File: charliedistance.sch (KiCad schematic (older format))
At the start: 1 part, among them X1 Badgelife_sao_connector_v169b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

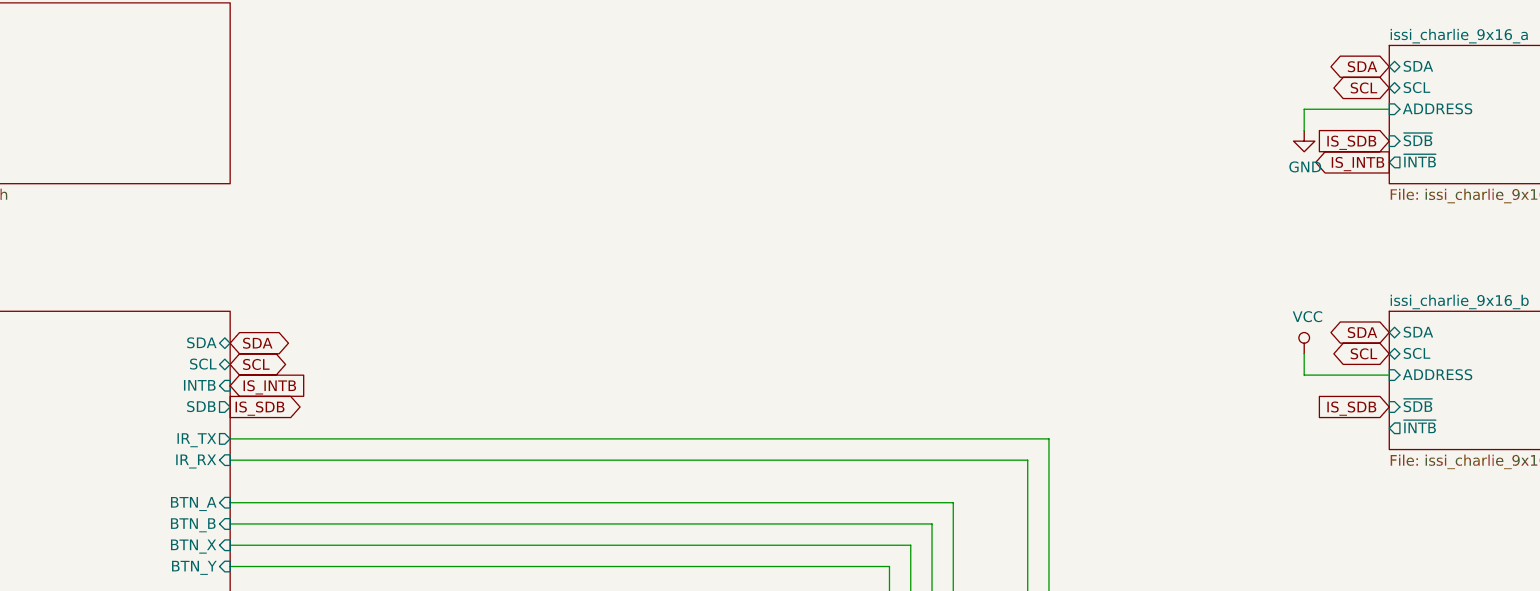
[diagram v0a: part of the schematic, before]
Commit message: Updates to production version
Changed infrared setup, added step-up for battery power, added battery power switch, added more capacitors, changed and added logos, etc.
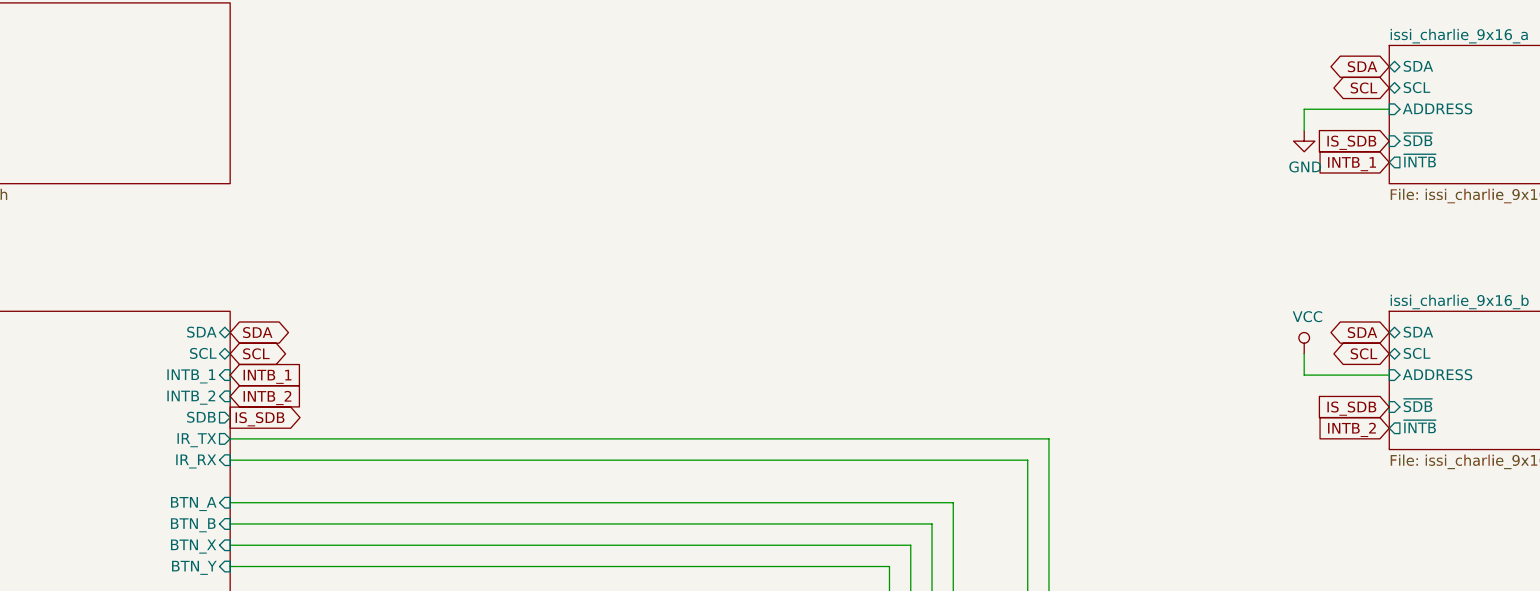
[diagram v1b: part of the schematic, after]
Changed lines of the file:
@@
 F2 "USB_BUS_POWER" I L 1100 1350 50
 $EndSheet
-Text GLabel 3100 2750 2    50   BiDi ~ 0
+Text GLabel 3100 2700 2    50   BiDi ~ 0
 SDA
-Text GLabel 3100 2850 2    50   BiDi ~ 0
+Text GLabel 3100 2800 2    50   BiDi ~ 0
 SCL
 Wire Wire Line
@@
 F1 "samd21.sch" 50
 F2 "USB_BUS_POWER" O L 1100 2800 50
-F3 "SDA" B R 3100 2750 50
-F4 "SCL" B R 3100 2850 50
+F3 "SDA" B R 3100 2700 50
+F4 "SCL" B R 3100 2800 50
 F5 "SAO_GPIO1" B R 3100 4000 50
 F6 "SAO_GPIO2" B R 3100 4100 50
@@
 F11 "BTN_X" I R 3100 3700 50
 F12 "BTN_Y" I R 3100 3800 50
-F13 "INTB" I R 3100 2950 50
-F14 "SDB" O R 3100 3050 50
+F13 "SDB" O R 3100 3100 50
+F14 "INTB_1" I R 3100 2900 50
+F15 "INTB_2" I R 3100 3000 50
 $EndSheet
 Wire Wire Line
@@
 Wire Wire Line
 	6200 5650 8550 5650
-Text GLabel 3100 3050 2    50   Output ~ 0
+Text GLabel 3100 3100 2    50   Output ~ 0
 IS_SDB
-Text GLabel 8550 1900 0    50   Output ~ 0
-IS_INTB
-Text GLabel 3100 2950 2    50   Input ~ 0
-IS_INTB
+Text GLabel 3100 2900 2    50   Input ~ 0
+INTB_1
+Text GLabel 3100 3000 2    50   Input ~ 0
+INTB_2
+Text GLabel 8550 1900 0    50   Input ~ 0
+INTB_1
+Text GLabel 8550 3150 0    50   Input ~ 0
+INTB_2
 $EndSCHEMATC
